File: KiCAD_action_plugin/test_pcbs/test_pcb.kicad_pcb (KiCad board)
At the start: 2 copper layers, 36.6 x 26.5 mm, 6 parts

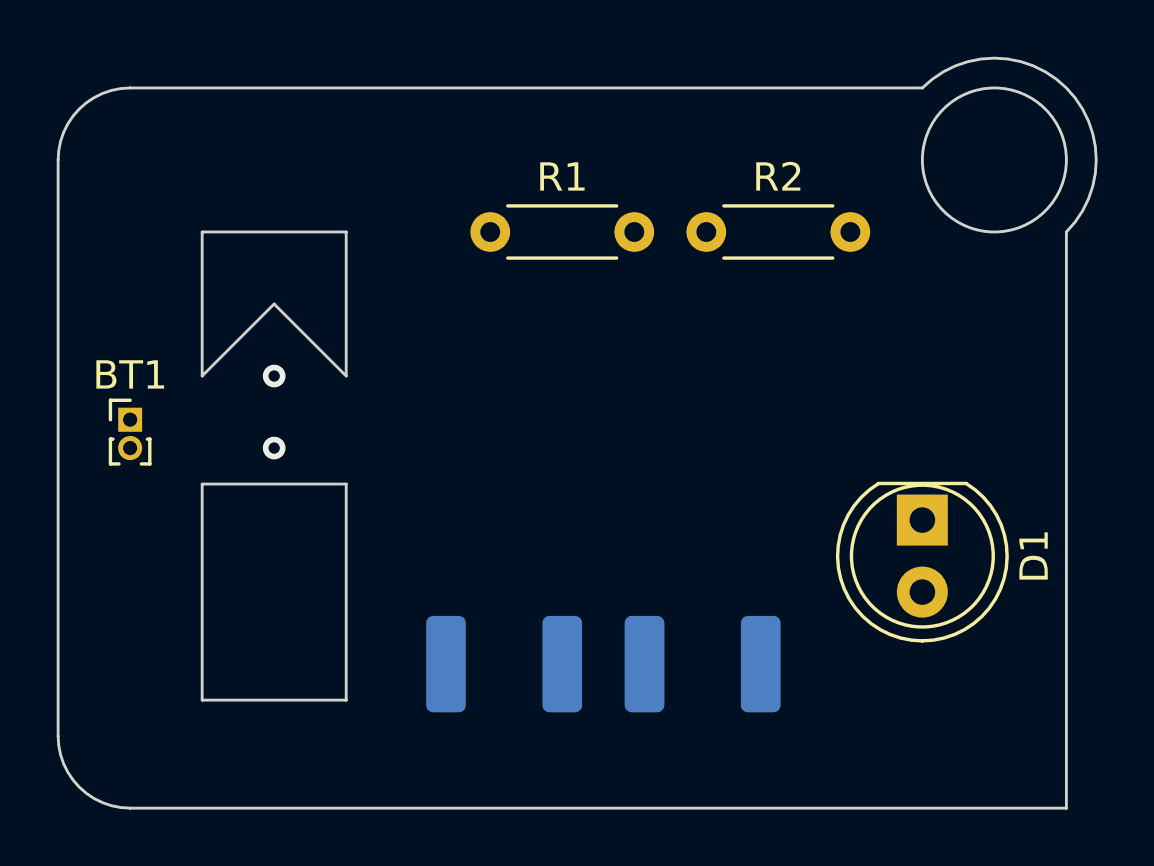
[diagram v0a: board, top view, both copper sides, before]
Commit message: Moved KiCAD plugin files to subdirectory
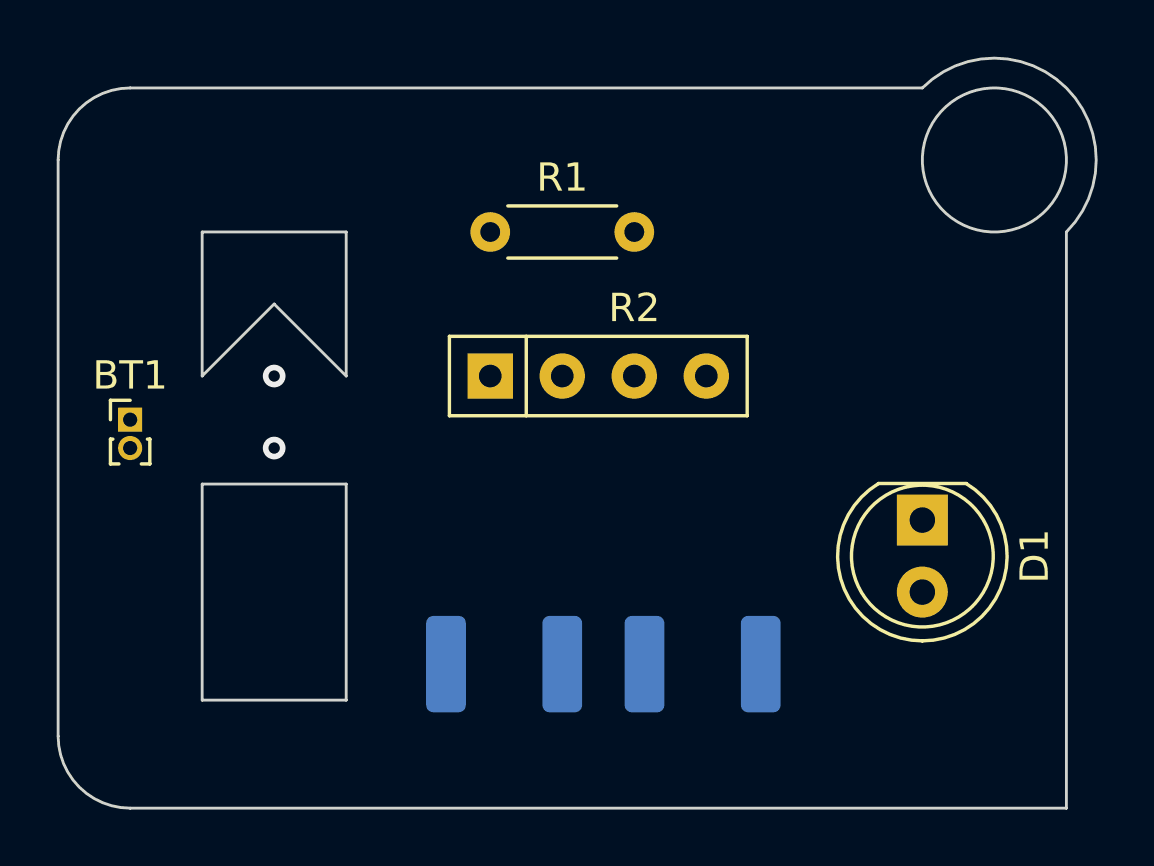
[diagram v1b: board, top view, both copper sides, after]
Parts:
- R2: footprint Resistor_THT:R_Axial_DIN0204_L3.6mm_D1.6mm_P5.08mm_Horizontal -> Resistor_THT:R_Array_SIP4
- moved R2 9.16 mm to (116.8, 71.1)
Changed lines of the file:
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@@
   (net 5 "Net-(BT1--)")
   (net 6 "Net-(R3-Pad2)")
-  (footprint "Resistor_THT:R_Axial_DIN0204_L3.6mm_D1.6mm_P5.08mm_Horizontal" (layer "F.Cu")
-    (at 124.46 66.04)
-    (descr "Resistor, Axial_DIN0204 series, Axial, Horizontal, pin pitch=5.08mm, 0.167W, length*diameter=3.6*1.6mm^2, http://cdn-reichelt.de/documents/datenblatt/B400/1_4W%23YAG.pdf")
-    (tags "Resistor Axial_DIN0204 series Axial Horizontal pin pitch 5.08mm 0.167W length 3.6mm diameter 1.6mm")
+  (footprint "Resistor_THT:R_Array_SIP4" (layer "F.Cu")
+    (at 116.84 71.12)
+    (descr "4-pin Resistor SIP pack")
+    (tags "R")
     (property "Sheetfile" "test_pcb.kicad_sch")
     (property "Sheetname" "")
@@
     (property "ki_keywords" "R res resistor")
     (attr through_hole)
-    (fp_text reference "R2" (at 2.54 -1.92) (layer "F.SilkS")
+    (fp_text reference "R2" (at 5.08 -2.4) (layer "F.SilkS")
         (effects (font (size 1 1) (thickness 0.15)))
     )
-    (fp_text value "R" (at 2.54 2.54) (layer "F.Fab")
+    (fp_text value "R" (at 5.08 2.4) (layer "F.Fab")
         (effects (font (size 1 1) (thickness 0.15)))
     )
-    (fp_text user "${REFERENCE}" (at 2.54 0) (layer "F.Fab")
-        (effects (font (size 0.72 0.72) (thickness 0.108)))
+    (fp_text user "${REFERENCE}" (at 3.81 0) (layer "F.Fab")
+        (effects (font (size 1 1) (thickness 0.15)))
     )
-    (fp_line (start 0.62 -0.92) (end 4.46 -0.92)
+    (fp_line (start -1.44 -1.4) (end -1.44 1.4)
       (stroke (width 0.12) (type solid)) (layer "F.SilkS"))
-    (fp_line (start 0.62 0.92) (end 4.46 0.92)
+    (fp_line (start -1.44 1.4) (end 9.06 1.4)
       (stroke (width 0.12) (type solid)) (layer "F.SilkS"))
-    (fp_line (start -0.95 -1.05) (end -0.95 1.05)
+    (fp_line (start 1.27 -1.4) (end 1.27 1.4)
+      (stroke (width 0.12) (type solid)) (layer "F.SilkS"))
+    (fp_line (start 9.06 -1.4) (end -1.44 -1.4)
+      (stroke (width 0.12) (type solid)) (layer "F.SilkS"))
+    (fp_line (start 9.06 1.4) (end 9.06 -1.4)
+      (stroke (width 0.12) (type solid)) (layer "F.SilkS"))
+    (fp_line (start -1.7 -1.65) (end -1.7 1.65)
       (stroke (width 0.05) (type solid)) (layer "F.CrtYd"))
-    (fp_line (start -0.95 1.05) (end 6.03 1.05)
+    (fp_line (start -1.7 1.65) (end 9.35 1.65)
       (stroke (width 0.05) (type solid)) (layer "F.CrtYd"))
-    (fp_line (start 6.03 -1.05) (end -0.95 -1.05)
+    (fp_line (start 9.35 -1.65) (end -1.7 -1.65)
       (stroke (width 0.05) (type solid)) (layer "F.CrtYd"))
-    (fp_line (start 6.03 1.05) (end 6.03 -1.05)
+    (fp_line (start 9.35 1.65) (end 9.35 -1.65)
       (stroke (width 0.05) (type solid)) (layer "F.CrtYd"))
-    (fp_line (start 0 0) (end 0.74 0)
+    (fp_line (start -1.29 -1.25) (end -1.29 1.25)
       (stroke (width 0.1) (type solid)) (layer "F.Fab"))
-    (fp_line (start 0.74 -0.8) (end 0.74 0.8)
+    (fp_line (start -1.29 1.25) (end 8.91 1.25)
       (stroke (width 0.1) (type solid)) (layer "F.Fab"))
-    (fp_line (start 0.74 0.8) (end 4.34 0.8)
+    (fp_line (start 1.27 -1.25) (end 1.27 1.25)
       (stroke (width 0.1) (type solid)) (layer "F.Fab"))
-    (fp_line (start 4.34 -0.8) (end 0.74 -0.8)
+    (fp_line (start 8.91 -1.25) (end -1.29 -1.25)
       (stroke (width 0.1) (type solid)) (layer "F.Fab"))
-    (fp_line (start 4.34 0.8) (end 4.34 -0.8)
+    (fp_line (start 8.91 1.25) (end 8.91 -1.25)
       (stroke (width 0.1) (type solid)) (layer "F.Fab"))
-    (fp_line (start 5.08 0) (end 4.34 0)
-      (stroke (width 0.1) (type solid)) (layer "F.Fab"))
-    (pad "1" thru_hole circle (at 0 0) (size 1.4 1.4) (drill 0.7) (layers "*.Cu" "*.Mask")
+    (pad "1" thru_hole rect (at 0 0) (size 1.6 1.6) (drill 0.8) (layers "*.Cu" "*.Mask")
       (net 4 "Net-(R1-Pad2)") (pintype "passive"))
-    (pad "2" thru_hole oval (at 5.08 0) (size 1.4 1.4) (drill 0.7) (layers "*.Cu" "*.Mask")
+    (pad "2" thru_hole oval (at 2.54 0) (size 1.6 1.6) (drill 0.8) (layers "*.Cu" "*.Mask")
       (net 2 "Net-(D1-A)") (pintype "passive"))
-    (model "${KICAD6_3DMODEL_DIR}/Resistor_THT.3dshapes/R_Axial_DIN0204_L3.6mm_D1.6mm_P5.08mm_Horizontal.wrl"
+    (pad "3" thru_hole oval (at 5.08 0) (size 1.6 1.6) (drill 0.8) (layers "*.Cu" "*.Mask"))
+    (pad "4" thru_hole oval (at 7.62 0) (size 1.6 1.6) (drill 0.8) (layers "*.Cu" "*.Mask"))
+    (model "${KICAD6_3DMODEL_DIR}/Resistor_THT.3dshapes/R_Array_SIP4.wrl"
       (offset (xyz 0 0 0))
       (scale (xyz 1 1 1))
